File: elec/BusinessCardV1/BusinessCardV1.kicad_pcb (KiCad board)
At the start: 2 copper layers, 176.2 x 54 mm, 102 parts, among them J1 61300411121, J2 6130XX11121_61300211121, Q1 DMG2305UX-7, Q2 DMG2305UX-7, Q3 DMG2305UX-7, Q4 DMG2305UX-7, Q5 DMG2305UX-7, Q6 DMG1012UW-7, Q7 DMG1012UW-7, Q8 DMG1012UW-7, U1 *, U10 SN74LVC08APWR, U11 SN74LVC08APWR, U12 SN74LVC08APWR, U13 SN74LVC08APWR, U14 MCP73831T-2DCI_OT, U15 TC4069UBFTEL_N, U16 SN74LVC1G139DCTR, U17 SN74LV161ADR, U18 ADXL327BCPZ, U19 TLV8544DR, U2 SN74LVC2G74DCTR, U20 TLC555CDR, U21 IQS228B00000000TSR, U3 TPS7A0233DBVR, U4 TLV8544DR, U5 TLV8544DR, U6 TC4069UBFTEL_N, U7 TC4069UBFTEL_N, U8 SN74LVC08APWR, U9 SN74LVC08APWR

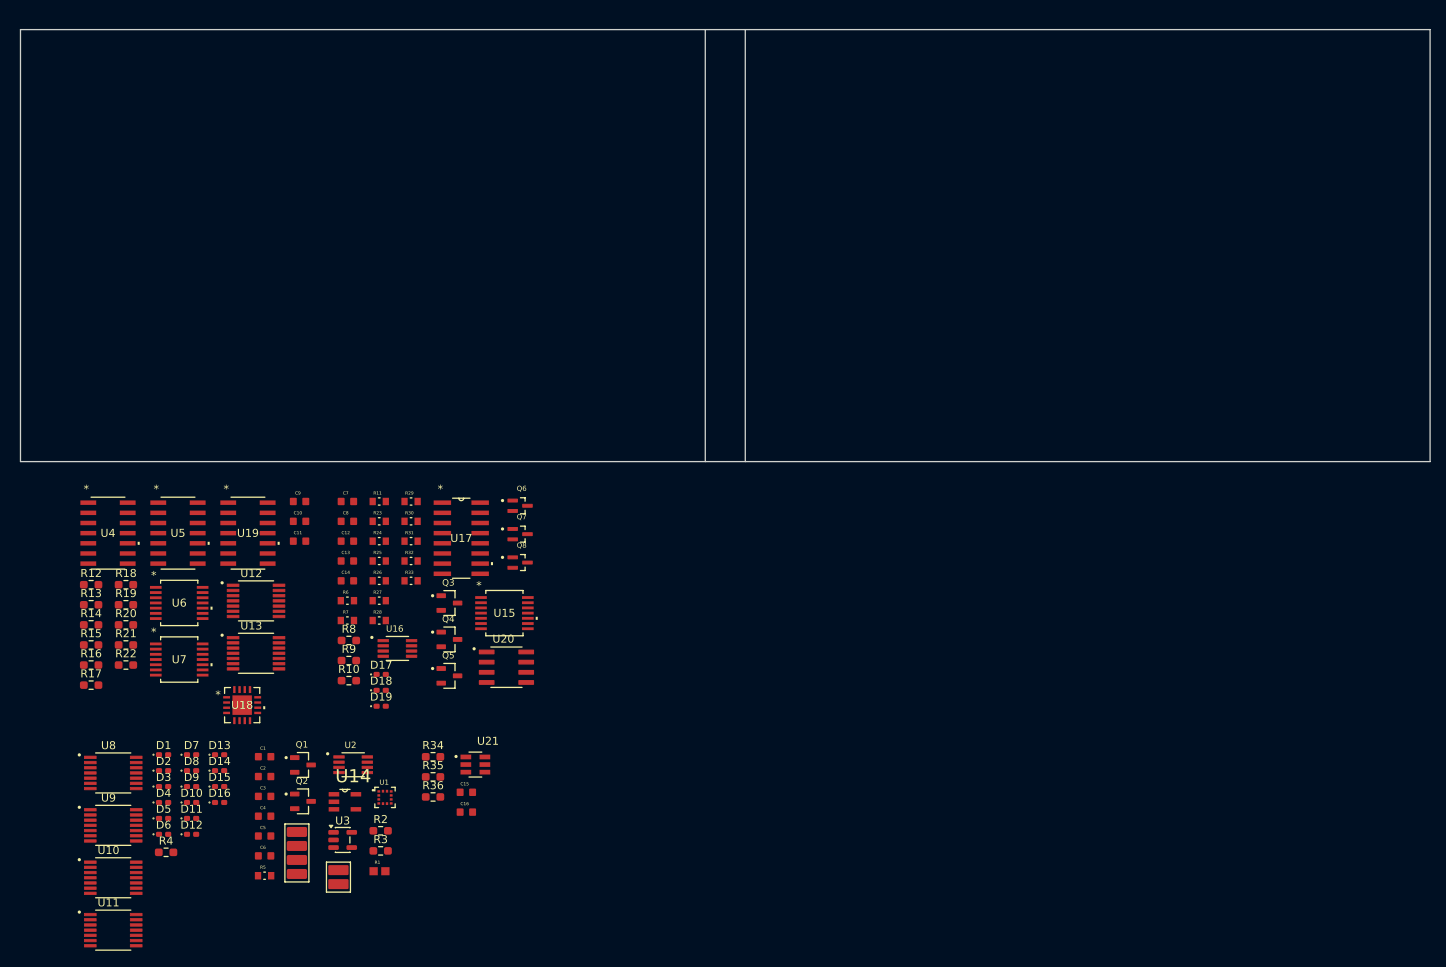
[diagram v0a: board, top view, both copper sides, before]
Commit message: pcb fix + round led layup
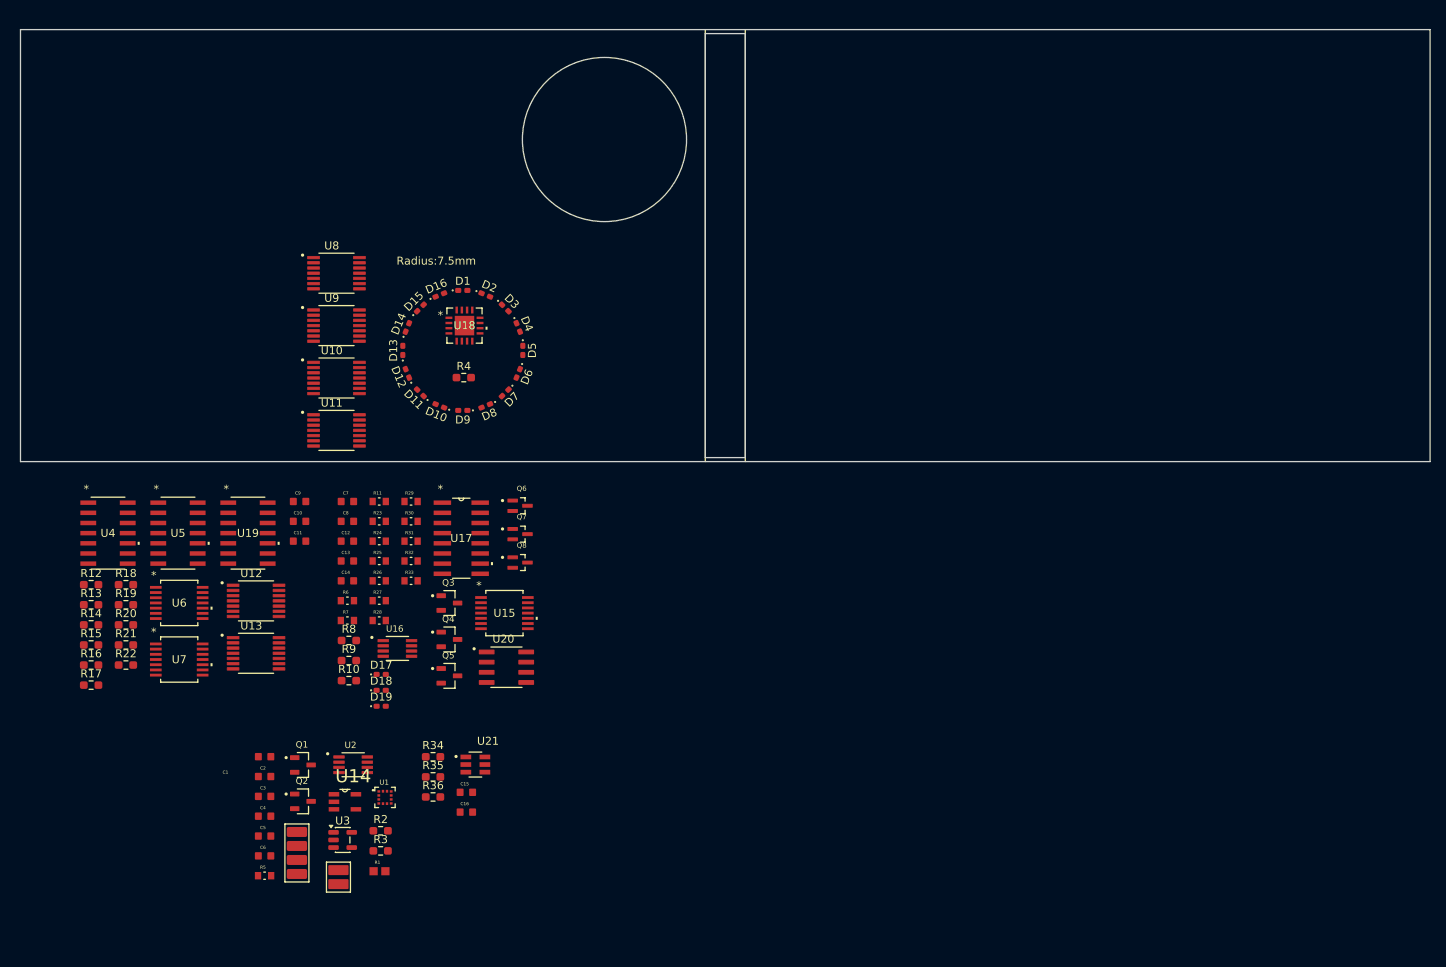
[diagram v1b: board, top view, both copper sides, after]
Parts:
- moved D4 74.1 mm to (82.7, 108.2), turned to -67.5 degrees
- moved D5 73.7 mm to (83.3, 111.1), turned to -90 degrees
- moved D3 73.5 mm to (81.1, 105.8), turned to -45 degrees
- moved D6 72.7 mm to (82.7, 114.0), turned to -112.5 degrees
- moved D2 71.8 mm to (78.7, 104.2), turned to -22.5 degrees
- moved R4 70.0 mm to (75.9, 114.5)
- moved D16 69.2 mm to (72.9, 104.2), turned to 22.5 degrees
- moved D1 69.0 mm to (75.8, 103.6)
- moved U10 68.4 mm to (60.0, 114.5)
- moved U11 68.4 mm to (60.0, 121.1)
- moved U9 68.4 mm to (60.0, 108.0)
- moved U8 68.4 mm to (60.0, 101.5)
- moved D15 64.9 mm to (70.5, 105.8), turned to 45 degrees
- moved D12 63.6 mm to (68.9, 114.0), turned to 112.5 degrees
- moved D11 60.4 mm to (70.5, 116.4), turned to 135 degrees
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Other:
- outline, holes or cut-outs redrawn
- board text added: "Radius:7.5mm"

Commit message: Started layout
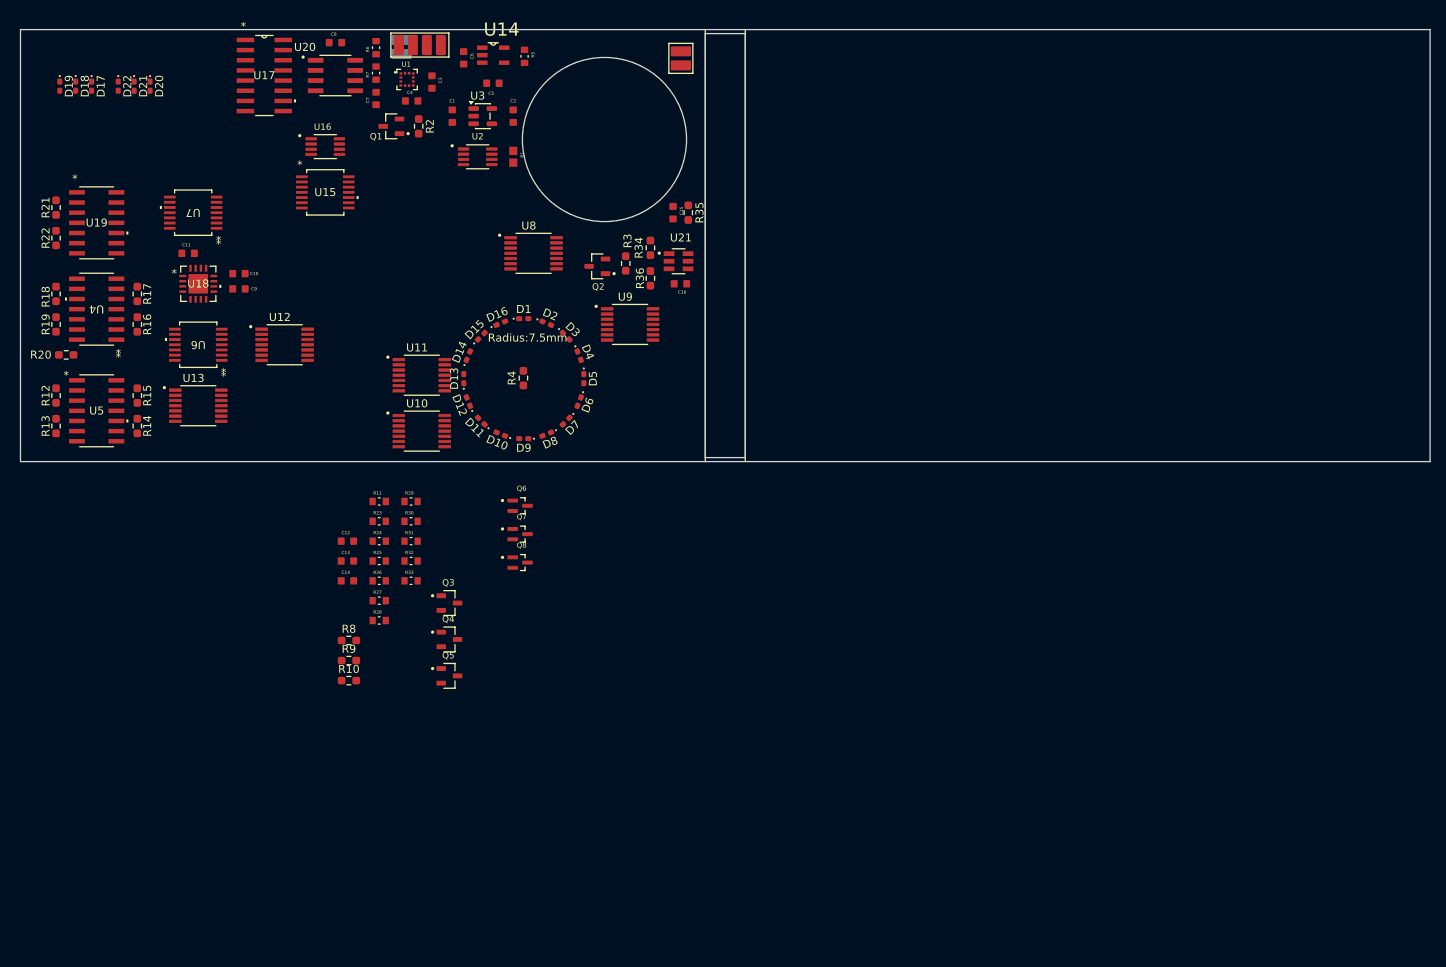
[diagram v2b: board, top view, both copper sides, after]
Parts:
- added D20: QBLP595-R, LED_SMD:LED_0402_1005Metric_Pad0.77x0.64mm_HandSolder, F.Cu at (36.7, 78.1)
- added D21: QBLP595-R, LED_SMD:LED_0402_1005Metric_Pad0.77x0.64mm_HandSolder, F.Cu at (34.7, 78.1)
- added D22: QBLP595-R, LED_SMD:LED_0402_1005Metric_Pad0.77x0.64mm_HandSolder, F.Cu at (32.7, 78.1)
- added J3: 6130XX11121_61300211121, Header1x2:Header1x2_SMD, F.Cu at (103.0, 73.7)
- J2: moved to B.Cu
- moved R5 107.5 mm to (83.5, 74.3), turned to -90 degrees
- moved J2 104.1 mm to (68.1, 72.3), turned to 180 degrees
- moved C6 102.8 mm to (75.9, 74.5), turned to -90 degrees
- moved J1 99.2 mm to (67.8, 72.9), turned to 90 degrees
- moved C5 98.3 mm to (79.6, 77.7)
- moved U14 95.1 mm to (79.6, 74.2)
- moved U3 92.2 mm to (78.3, 81.8)
- moved C3 91.7 mm to (71.9, 77.6), turned to -90 degrees
- moved C4 91.3 mm to (69.4, 79.9)
- moved R1 90.9 mm to (82.1, 86.9), turned to -90 degrees
- moved U1 89.8 mm to (68.8, 77.2)
- moved C2 88.2 mm to (82.1, 81.8), turned to 90 degrees
- moved R2 88.2 mm to (70.3, 83.1), turned to -90 degrees
- moved D19 87.3 mm to (25.4, 78.1), turned to -90 degrees
- moved D18 84.6 mm to (27.4, 78.1), turned to -90 degrees
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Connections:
- C8 pad 2: +3.3V -> /RGB_LED_Circuit/Power3V3

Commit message: Position made, but kicad lagging everytime i add a wire
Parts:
- added U22: TPD12S520DBT, PCBArt:design, F.Cu at (153.8, 98.0)
- moved Q5 86.3 mm to (37.6, 73.6)
- moved R10 83.3 mm to (34.5, 73.6), turned to 90 degrees
- moved Q3 82.5 mm to (26.2, 75.5)
- moved R8 81.9 mm to (22.4, 75.5), turned to 90 degrees
- moved Q4 72.5 mm to (41.5, 82.5)
- moved Q6 72.0 mm to (32.6, 79.1)
- moved R28 71.8 mm to (40.8, 77.4), turned to -90 degrees
- moved R9 71.3 mm to (38.3, 82.5), turned to 90 degrees
- moved R25 70.4 mm to (25.6, 79.3), turned to 90 degrees
- moved R27 70.2 mm to (38.9, 77.4), turned to 90 degrees
- moved Q7 68.8 mm to (44.0, 77.4)
- moved R26 68.7 mm to (37.0, 77.4), turned to 90 degrees
- moved R23 64.3 mm to (29.3, 79.2), turned to -90 degrees
- moved C12 63.9 mm to (26.2, 81.6)
- moved R11 63.3 mm to (27.4, 79.2), turned to 90 degrees
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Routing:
- net +3.3V: track 0.00 -> 24.9 mm

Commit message: Push before destroying everything
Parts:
- removed U22: TPD12S520DBT, PCBArt:design
- moved J2 4.95 mm to (73.1, 72.2)
- moved R1 1.14 mm to (81.0, 86.9)
- moved U2 1.14 mm to (76.5, 86.9)
- moved J1 0.25 mm to (67.8, 73.2)
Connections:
- C8 pad 2: /RGB_LED_Circuit/Power3V3 -> Power3V3
- J3 pad 2: +3.3V -> /Power/V_Bat
- Q1 pad 3: /Power/Power3V3 -> Power3V3
- Q3 pad 2: /RGB_LED_Circuit/Power3V3 -> Power3V3
- Q4 pad 2: /RGB_LED_Circuit/Power3V3 -> Power3V3
- Q5 pad 2: /RGB_LED_Circuit/Power3V3 -> Power3V3
- R10 pad 1: /RGB_LED_Circuit/Power3V3 -> Power3V3
- R24 pad 1: /RGB_LED_Circuit/Power3V3 -> Power3V3
- R29 pad 1: /RGB_LED_Circuit/Power3V3 -> Power3V3
- R33 pad 1: /RGB_LED_Circuit/Power3V3 -> Power3V3
- R6 pad 2: /RGB_LED_Circuit/Power3V3 -> Power3V3
- R8 pad 1: /RGB_LED_Circuit/Power3V3 -> Power3V3
- R9 pad 1: /RGB_LED_Circuit/Power3V3 -> Power3V3
- U15 pad 14: /RGB_LED_Circuit/Power3V3 -> Power3V3
- U16 pad 8: /RGB_LED_Circuit/Power3V3 -> Power3V3
- U17 pad 1: /RGB_LED_Circuit/Power3V3 -> Power3V3
- U17 pad 10: /RGB_LED_Circuit/Power3V3 -> Power3V3
- U17 pad 16: /RGB_LED_Circuit/Power3V3 -> Power3V3
- U17 pad 7: /RGB_LED_Circuit/Power3V3 -> Power3V3
- U20 pad 4: /RGB_LED_Circuit/Power3V3 -> Power3V3
- U20 pad 8: /RGB_LED_Circuit/Power3V3 -> Power3V3
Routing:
- net +3.3V: track 24.9 -> 71.5 mm
- net /Power/V_Bat: track 0.00 -> 44.3 mm
- net /Power/SolarPower: track 0.00 -> 18.5 mm, vias 0 -> 1
- net /Power/INT_CLK: track 0.00 -> 12.5 mm, vias 0 -> 2
- net /Power/SDX: track 0.00 -> 10.4 mm
- net Power3V3: track 0.00 -> 7.28 mm
- net /Power/~{CSB}: track 0.00 -> 4.41 mm
- net /Power/SCX: track 0.00 -> 4.19 mm
- net /Power/SDO: track 0.00 -> 3.41 mm
- net Net-(U14-PROG): track 0.00 -> 2.65 mm

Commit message: Easy part done, Glabel kind of worked
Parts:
- moved Q8 14.8 mm to (35.8, 83.0), turned to 180 degrees
- moved Q7 10.9 mm to (33.3, 75.0), turned to 180 degrees
- moved R10 10.7 mm to (44.5, 77.2), turned to -90 degrees
- moved R8 10.6 mm to (32.2, 79.5), turned to -90 degrees
- moved Q6 10.6 mm to (22.7, 75.4), turned to 180 degrees
- moved R9 10.3 mm to (47.9, 86.2), turned to -90 degrees
- moved C12 9.87 mm to (29.0, 72.2), turned to 180 degrees
- moved R32 8.59 mm to (39.0, 83.0), turned to 90 degrees
- moved C14 7.90 mm to (42.2, 80.5), turned to 180 degrees
- moved C13 7.75 mm to (37.5, 72.2), turned to 180 degrees
- moved R25 5.75 mm to (29.6, 75.2), turned to -90 degrees
- moved R26 5.70 mm to (41.1, 73.4), turned to -90 degrees
- moved Q5 5.21 mm to (41.3, 77.2), turned to 180 degrees
- moved R23 5.19 mm to (25.9, 75.3), turned to 90 degrees
- moved R31 5.09 mm to (40.9, 83.0), turned to -90 degrees
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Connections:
- net /Accelerometer_Circle_Setup/ADXL_X_OUT renamed ADXL_X_OUT
- net /Accelerometer_Circle_Setup/ADXL_Y_OUT renamed ADXL_Y_OUT
- net /Accelerometer_Circle_Setup/op_y2 renamed op_y2
- net /Accelerometer_Circle_Setup/op_y3 renamed op_y3
- net /Accelerometer_Circle_Setup/op_y4 renamed op_y4
- net /Accelerometer_Circle_Setup/op_y5 renamed op_y5
- net /Accelerometer_Circle_Setup/op_y6 renamed op_y6
- net /Accelerometer_Circle_Setup/op_y7 renamed op_y7
- net /Accelerometer_Circle_Setup/op_y8 renamed op_y8
- net /Accelerometer_Circle_Setup/~{y1} renamed ~{y1}
- net /Accelerometer_Circle_Setup/~{y2} renamed ~{y2}
- net /Accelerometer_Circle_Setup/~{y3} renamed ~{y3}
- net /Accelerometer_Circle_Setup/~{y4} renamed ~{y4}
- net /Accelerometer_Circle_Setup/~{y5} renamed ~{y5}
- net /Accelerometer_Circle_Setup/~{y6} renamed ~{y6}
- net /Accelerometer_Circle_Setup/~{y7} renamed ~{y7}
- net /Power/INT_CLK renamed INT_CLK
- net /Power/Q renamed Q
- net /Power/RingBTN renamed RingBTN
- net /Power/SCX renamed SCX
- net /Power/SDO renamed SDO
- net /Power/SDX renamed SDX
- net /Power/SolarPower renamed SolarPower
- net /Power/V_Bat renamed V_Bat
- net /Power/~{CSB} renamed ~{CSB}
- net /Power/~{Q} renamed ~{Q}
- net /RGB_LED_Circuit/CLK_Sequence renamed CLK_Sequence
- net /RGB_LED_Circuit/Charge_Blue_Cap renamed Charge_Blue_Cap
- net /RGB_LED_Circuit/Charge_Green_Cap renamed Charge_Green_Cap
- net /RGB_LED_Circuit/Charge_Red_Cap renamed Charge_Red_Cap
- net /RGB_LED_Circuit/DISCH renamed DISCH
- net /RGB_LED_Circuit/Green_LED renamed Green_LED
- net /RGB_LED_Circuit/LSB_Counter renamed LSB_Counter
- net /RGB_LED_Circuit/MSB_Counter renamed MSB_Counter
- net /RGB_LED_Circuit/Reset renamed Reset
- net /RGB_LED_Circuit/TRIG renamed TRIG
- net /RGB_LED_Circuit/~{Blue_LED} renamed ~{Blue_LED}
- net /RGB_LED_Circuit/~{Green_LED} renamed ~{Green_LED}
- net /RGB_LED_Circuit/~{Red_LED} renamed ~{Red_LED}
- net /RGB_LED_Circuit/~{Reset} renamed ~{Reset}
- C11 pad 2: /Accelerometer_Circle_Setup/RingPower -> RingPower
- Q2 pad 3: /Power/RingPower -> RingPower
- R12 pad 1: /Accelerometer_Circle_Setup/RingPower -> RingPower
- R21 pad 1: /Accelerometer_Circle_Setup/RingPower -> RingPower
- U10 pad 1: /Accelerometer_Circle_LED/~{x} -> ~{x}
- U10 pad 10: /Accelerometer_Circle_LED/Y3 -> Y3
- U10 pad 12: /Accelerometer_Circle_LED/~{x} -> ~{x}
- U10 pad 13: /Accelerometer_Circle_LED/Y4 -> Y4
- U10 pad 14: /Accelerometer_Circle_LED/RingPower -> RingPower
- U10 pad 2: /Accelerometer_Circle_LED/Y1 -> Y1
- U10 pad 4: /Accelerometer_Circle_LED/~{x} -> ~{x}
- U10 pad 5: /Accelerometer_Circle_LED/Y2 -> Y2
- U10 pad 9: /Accelerometer_Circle_LED/~{x} -> ~{x}
- U11 pad 1: /Accelerometer_Circle_LED/~{x} -> ~{x}
- U11 pad 10: /Accelerometer_Circle_LED/Y7 -> Y7
- U11 pad 12: /Accelerometer_Circle_LED/~{x} -> ~{x}
- U11 pad 13: /Accelerometer_Circle_LED/Y8 -> Y8
- U11 pad 14: /Accelerometer_Circle_LED/RingPower -> RingPower
- U11 pad 2: /Accelerometer_Circle_LED/Y5 -> Y5
- U11 pad 4: /Accelerometer_Circle_LED/~{x} -> ~{x}
- U11 pad 5: /Accelerometer_Circle_LED/Y6 -> Y6
- U11 pad 9: /Accelerometer_Circle_LED/~{x} -> ~{x}
- U12 pad 11: /Accelerometer_Circle_Setup/Y5 -> Y5
- U12 pad 14: /Accelerometer_Circle_Setup/RingPower -> RingPower
- U12 pad 3: /Accelerometer_Circle_Setup/Y2 -> Y2
- U12 pad 6: /Accelerometer_Circle_Setup/Y3 -> Y3
- U12 pad 8: /Accelerometer_Circle_Setup/Y4 -> Y4
- U13 pad 14: /Accelerometer_Circle_Setup/RingPower -> RingPower
- U13 pad 3: /Accelerometer_Circle_Setup/Y6 -> Y6
- U13 pad 6: /Accelerometer_Circle_Setup/Y7 -> Y7
- U13 pad 8: /Accelerometer_Circle_Setup/Y8 -> Y8
- U15 pad 11: /RGB_LED_Circuit/Red_LED -> Red_LED
- U15 pad 5: /RGB_LED_Circuit/Blue_LED -> Blue_LED
- U16 pad 5: /RGB_LED_Circuit/Blue_LED -> Red_LED
- U16 pad 7: /RGB_LED_Circuit/Red_LED -> Blue_LED
- U18 pad 14: /Accelerometer_Circle_Setup/RingPower -> RingPower
- U18 pad 15: /Accelerometer_Circle_Setup/RingPower -> RingPower
- U19 pad 1: /Accelerometer_Circle_Setup/x -> x
- U19 pad 4: /Accelerometer_Circle_Setup/RingPower -> RingPower
- U4 pad 4: /Accelerometer_Circle_Setup/RingPower -> RingPower
- U5 pad 1: /Accelerometer_Circle_Setup/Y1 -> Y1
- U5 pad 4: /Accelerometer_Circle_Setup/RingPower -> RingPower
- U6 pad 1: /Accelerometer_Circle_Setup/Y1 -> Y1
- U6 pad 14: /Accelerometer_Circle_Setup/RingPower -> RingPower
- U7 pad 14: /Accelerometer_Circle_Setup/RingPower -> RingPower
- U7 pad 3: /Accelerometer_Circle_Setup/x -> x
- U7 pad 4: /Accelerometer_Circle_Setup/~{x} -> ~{x}
- U8 pad 1: /Accelerometer_Circle_LED/x -> x
- U8 pad 10: /Accelerometer_Circle_LED/Y3 -> Y3
- U8 pad 12: /Accelerometer_Circle_LED/x -> x
- U8 pad 13: /Accelerometer_Circle_LED/Y4 -> Y4
- U8 pad 14: /Accelerometer_Circle_LED/RingPower -> RingPower
- U8 pad 2: /Accelerometer_Circle_LED/Y1 -> Y1
- U8 pad 4: /Accelerometer_Circle_LED/x -> x
- U8 pad 5: /Accelerometer_Circle_LED/Y2 -> Y2
- U8 pad 9: /Accelerometer_Circle_LED/x -> x
- U9 pad 1: /Accelerometer_Circle_LED/x -> x
- U9 pad 10: /Accelerometer_Circle_LED/Y7 -> Y7
- U9 pad 12: /Accelerometer_Circle_LED/x -> x
- U9 pad 13: /Accelerometer_Circle_LED/Y8 -> Y8
- U9 pad 14: /Accelerometer_Circle_LED/RingPower -> RingPower
- U9 pad 2: /Accelerometer_Circle_LED/Y5 -> Y5
- U9 pad 4: /Accelerometer_Circle_LED/x -> x
- U9 pad 5: /Accelerometer_Circle_LED/Y6 -> Y6
- U9 pad 9: /Accelerometer_Circle_LED/x -> x
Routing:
- net Power3V3: track 7.28 -> 120.0 mm, vias 0 -> 2
- net RingPower: track 0.00 -> 32.3 mm
- net ~{Blue_LED}: track 0.00 -> 31.5 mm, vias 0 -> 2
- net ~{Green_LED}: track 0.00 -> 28.8 mm, vias 0 -> 2
- net Blue_LED: track 0.00 -> 23.9 mm
- net Net-(D18-CATHODE_(-)): track 0.00 -> 22.1 mm
- net Net-(D17-CATHODE_(-)): track 0.00 -> 20.7 mm
- net ~{Red_LED}: track 0.00 -> 20.6 mm, vias 0 -> 2
- net CLK_Sequence: track 0.00 -> 20.1 mm
- net Net-(D19-CATHODE_(-)): track 0.00 -> 16.2 mm
- net ~{Reset}: track 0.00 -> 14.7 mm
- net Green_LED: track 0.00 -> 13.5 mm
- net LSB_Counter: track 0.00 -> 11.1 mm
- net Red_LED: track 0.00 -> 11.0 mm
- net MSB_Counter: track 0.00 -> 10.8 mm
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
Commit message: PCB routed
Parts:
- added C17: 1uf, CL10B105KP8NNNC:CAPC1608X90N, F.Cu at (58.3, 97.8)
- added C18: 1uf, CL10B105KP8NNNC:CAPC1608X90N, F.Cu at (54.8, 106.7)
- added C19: 1uf, CL10B105KP8NNNC:CAPC1608X90N, F.Cu at (54.3, 114.3)
- added C20: 1uf, CL10B105KP8NNNC:CAPC1608X90N, F.Cu at (42.6, 114.3)
- added C21: 1uf, CL10B105KP8NNNC:CAPC1608X90N, F.Cu at (51.2, 84.4)
- added C22: 1uf, CL10B105KP8NNNC:CAPC1608X90N, F.Cu at (58.6, 82.8)
- added C23: 1uf, CL10B105KP8NNNC:CAPC1608X90N, F.Cu at (60.9, 89.2)
- added J4: 6130XX11121_61300211121, Header1x2:Header1x2_SMD, F.Cu at (102.2, 109.8)
- added R37: 0, Resistor_SMD:R_0603_1608Metric_Pad0.98x0.95mm_HandSolder, F.Cu at (103.0, 105.4)
- moved U18 0.88 mm to (41.9, 103.1), turned to 11.25 degrees
- moved C2 0.85 mm to (81.7, 81.1)
- moved C16 0.63 mm to (103.0, 103.4)
- moved U14 0.51 mm to (79.6, 74.7)
- moved U5 0.25 mm to (30.0, 118.4)
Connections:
- R34 pad 1: /Buttons/RingBTN -> RingBTN
- R36 pad 1: /Buttons/RingBTN -> RingBTN
- U21 pad 6: /Buttons/TouchSensor -> TouchSensor
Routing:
- net RingPower: track 32.3 -> 182.3 mm, vias 0 -> 3
- net x: track 0.00 -> 111.0 mm, vias 0 -> 4
- net Net-(D1-CATHODE_(-)): track 0.00 -> 100.9 mm
- net Y6: track 0.00 -> 79.4 mm, vias 0 -> 3
- net Y7: track 0.00 -> 76.9 mm, vias 0 -> 4
- net Y1: track 0.00 -> 75.5 mm, vias 0 -> 6
- net Y8: track 0.00 -> 73.8 mm, vias 0 -> 4
- net GND: track 0.00 -> 70.1 mm, vias 0 -> 246
- net Y2: track 0.00 -> 67.5 mm, vias 0 -> 3
- net Y4: track 0.00 -> 64.6 mm, vias 0 -> 2
- net ~{x}: track 0.00 -> 61.0 mm, vias 0 -> 3
- net Y3: track 0.00 -> 55.5 mm, vias 0 -> 3
- net ADXL_Y_OUT: track 2.49 -> 55.9 mm, vias 0 -> 2
- net Y5: track 0.00 -> 50.6 mm, vias 0 -> 4
- net op_y7: track 0.00 -> 47.4 mm, vias 0 -> 3
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- added copper zone on B.Cu, net GND
- added copper zone on F.Cu, net GND
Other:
- board text removed: "Radius:7.5mm"

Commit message: pcb art
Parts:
- added U22: TPD12S520DBT, PCBArt:design, F.Cu at (153.8, 98.0)
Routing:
- net (no net): vias 0 -> 2
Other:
- outline, holes or cut-outs redrawn
- board text added: "GND"
- board text added: "Pad"
- board text added: "TouchSensor"
